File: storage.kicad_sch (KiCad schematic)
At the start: 18 parts, among them J6 Micro_SD_Card_Det1, U1 MIMX8MM6DVTLZAA, U27 TPD4EUSB30, U28 D5V0H1B2LP, U29 W25Q32JWZP, U30 SiP32431DR3, U31 TPD4EUSB30

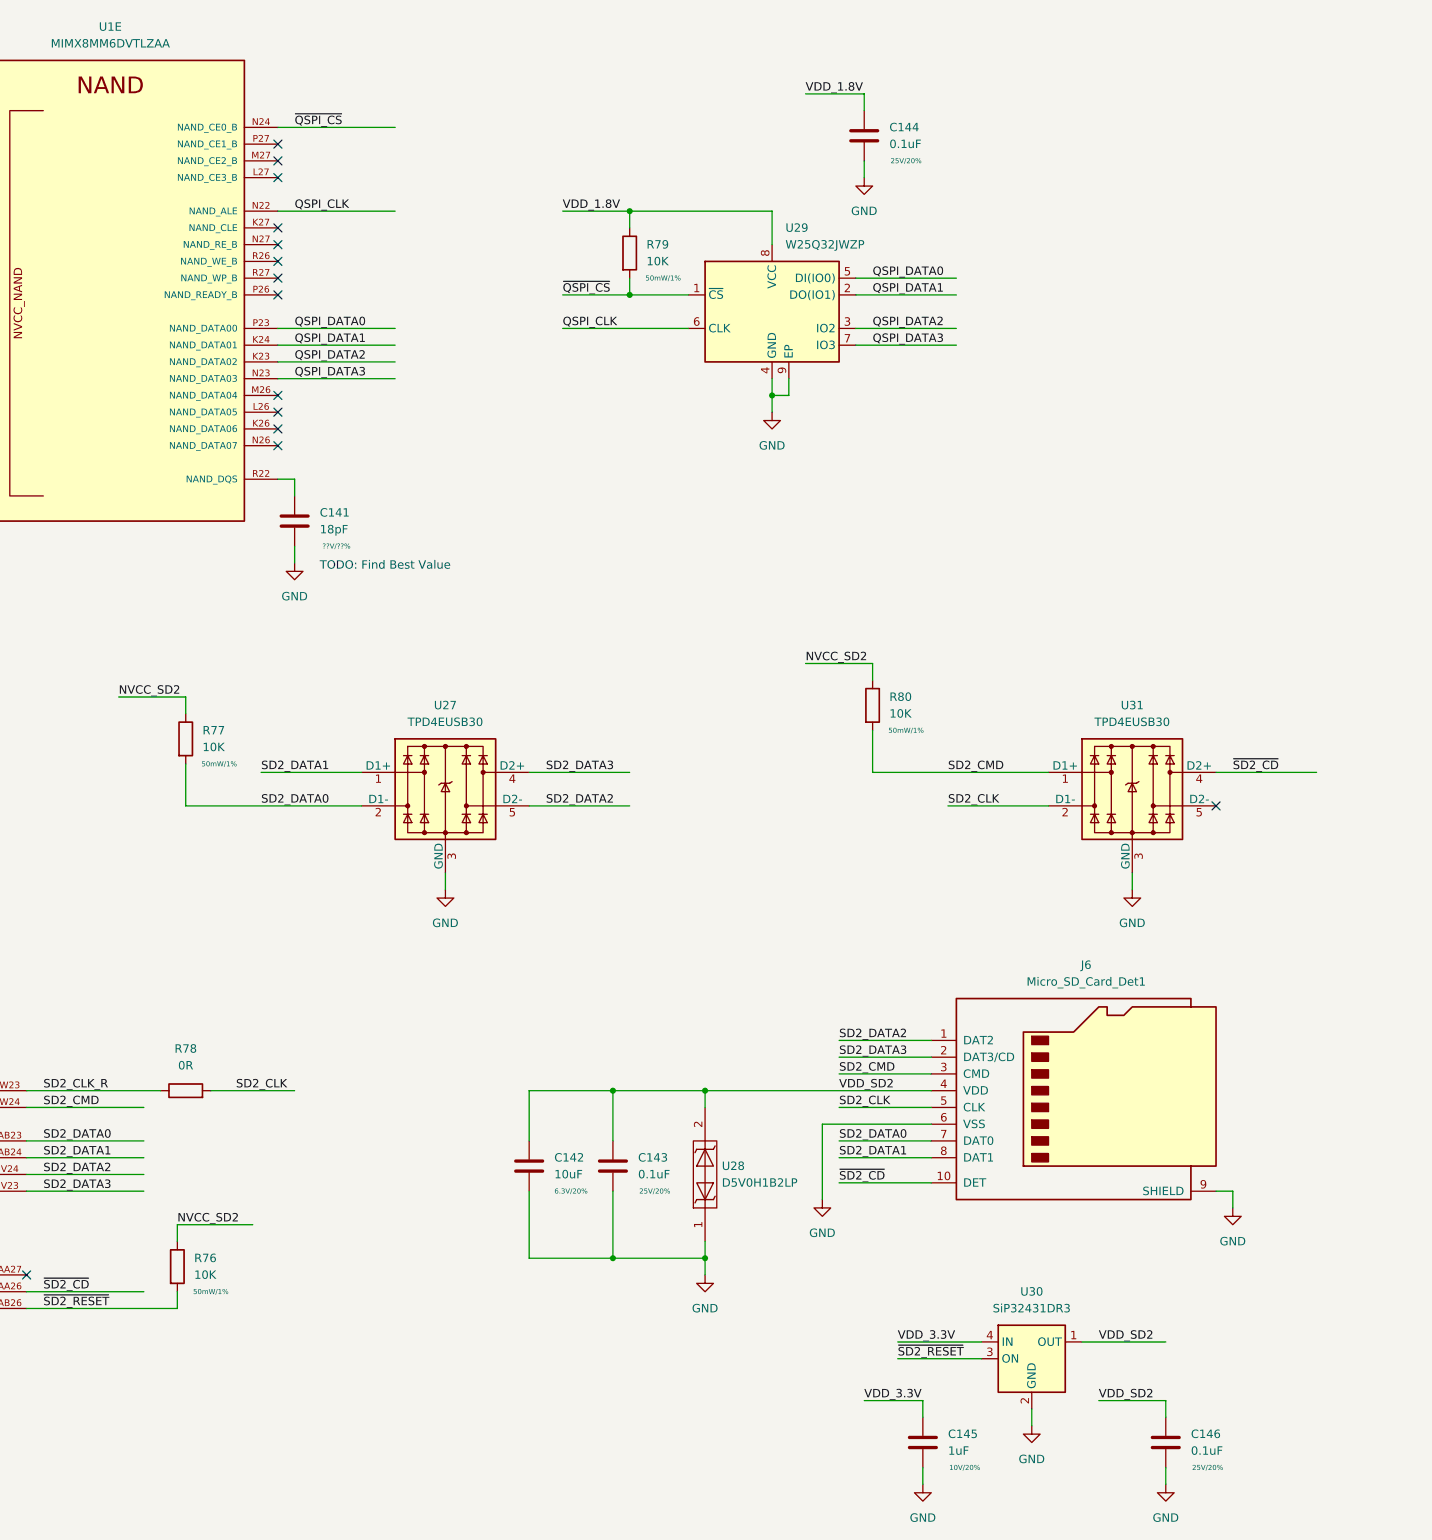
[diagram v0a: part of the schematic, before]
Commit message: v2 of ddr flytimes tool, lots of routing work, sch fixes
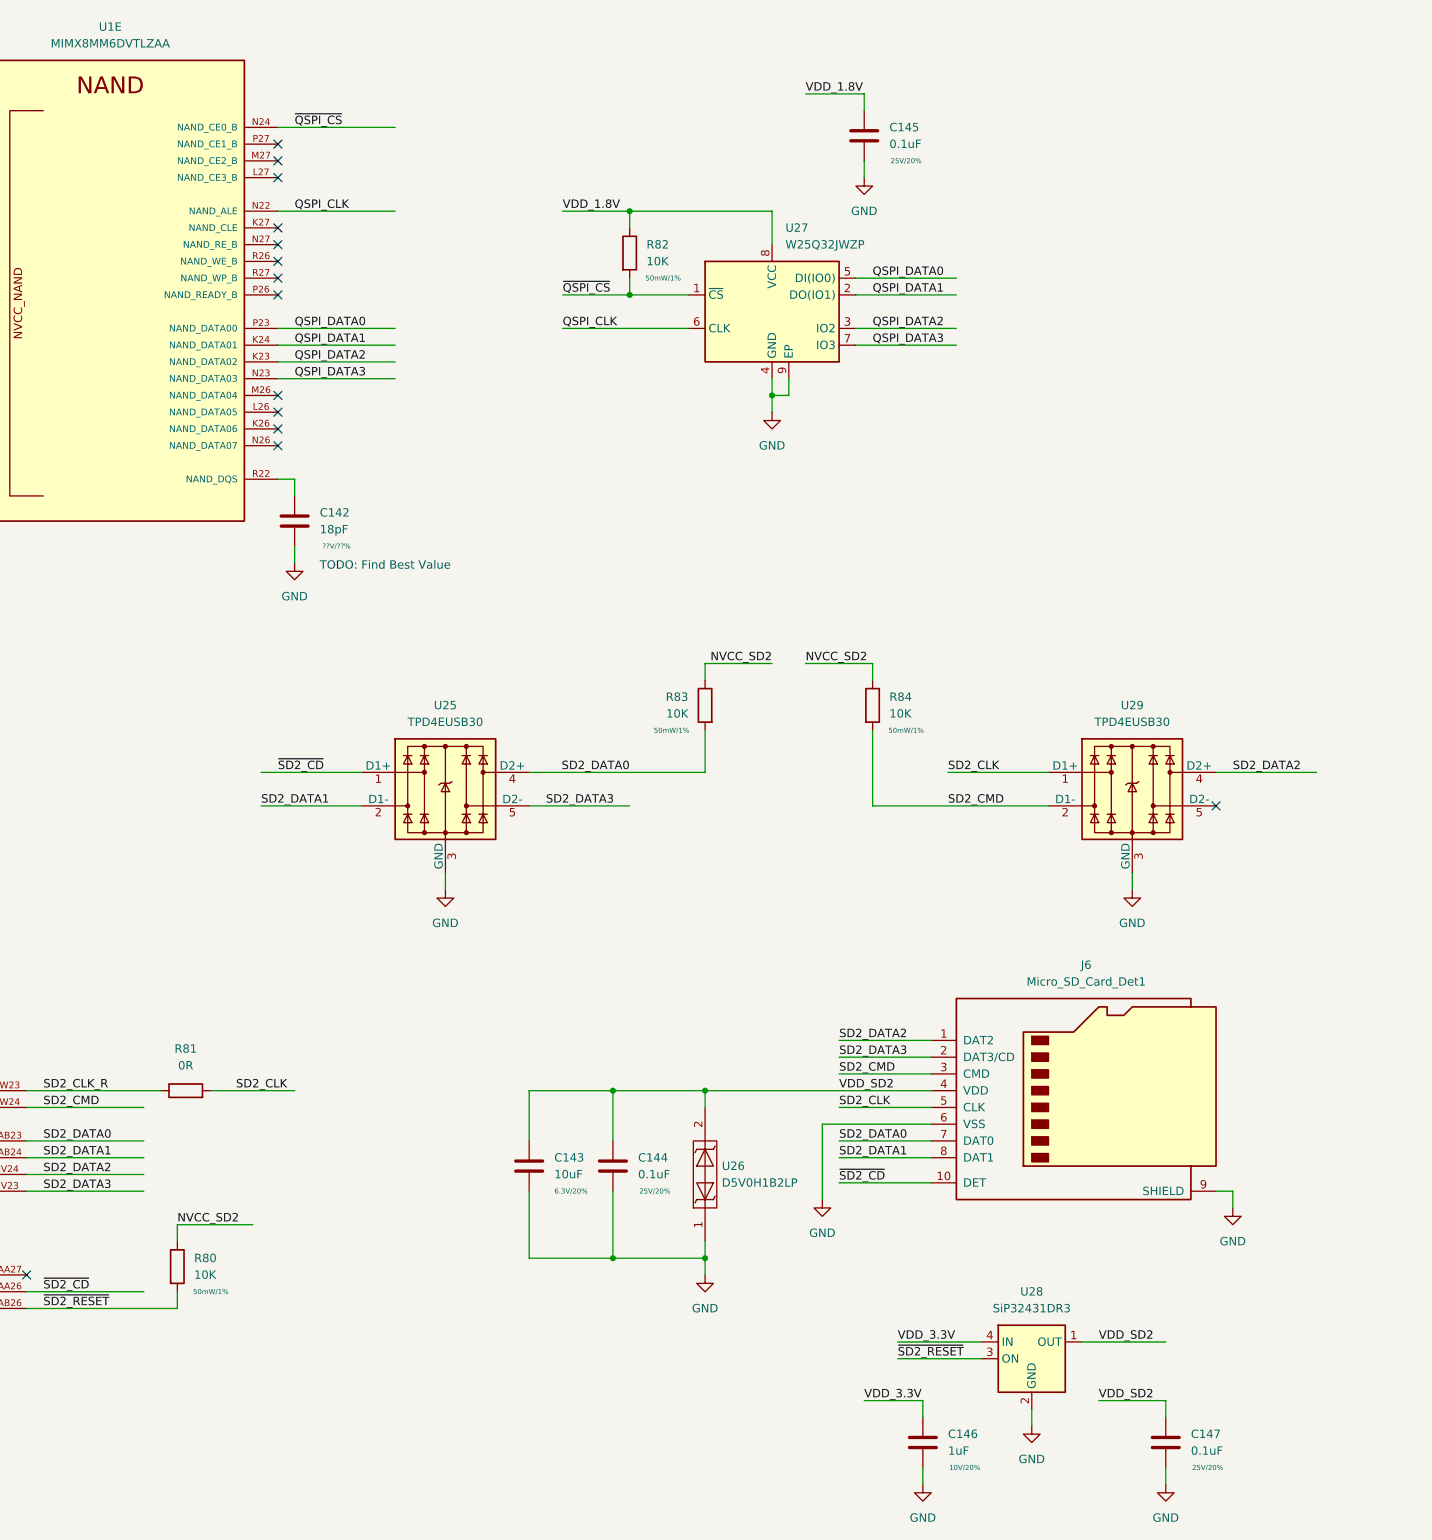
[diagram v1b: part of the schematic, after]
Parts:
- C142: renamed from C141; footprint Capacitor_SMD:C_0402_1005Metric -> qsbc:C_0201_0603Metric
- R81: renamed from R78; footprint Resistor_SMD:R_0402_1005Metric -> qsbc:R_0201_0603Metric
- renumbered C142 to C143, C143 to C144, C144 to C145, C145 to C146, C146 to C147, R76 to R80, R79 to R82, R77 to R83, R80 to R84, U27 to U25, U28 to U26, U29 to U27, U30 to U28, U31 to U29
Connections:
- net SD2_CLK: now also U29.1 (D1+), U29.10; no longer U29.2 (D1-), U29.9
- net SD2_CMD: now also U29.2 (D1-), U29.9; no longer U29.1 (D1+), U29.10
- net SD2_DATA0: now also U25.4 (D2+), U25.7; no longer U25.2 (D1-), U25.9
- net SD2_DATA1: now also U25.2 (D1-), U25.9; no longer U25.1 (D1+), U25.10
- net SD2_DATA2: now also U29.4 (D2+), U29.7; no longer U25.5 (D2-), U25.6
- net SD2_DATA3: now also U25.5 (D2-), U25.6; no longer U25.4 (D2+), U25.7
- net ~{SD2_CD}: now also U25.1 (D1+), U25.10; no longer U29.4 (D2+), U29.7
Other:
- moved on the sheet: R83

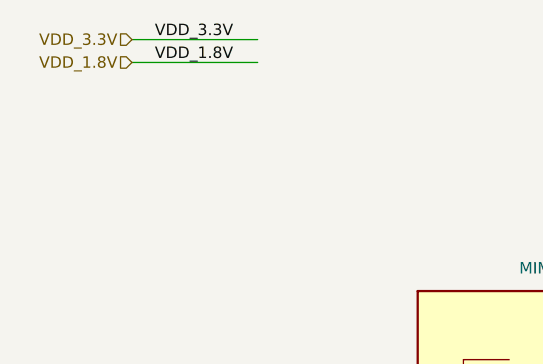
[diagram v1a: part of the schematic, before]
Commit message: more routing work, prepare to change to x32 lpddr4
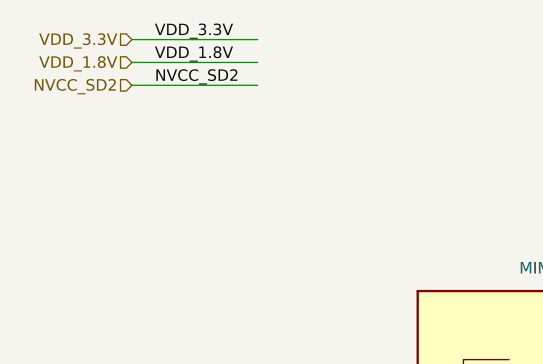
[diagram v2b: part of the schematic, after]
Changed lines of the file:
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@@
+    (stroke (width 0) (type default) (color 0 0 0 0))
+  )
+  (wire (pts (xy 29.21 24.13) (xy 43.18 24.13))
     (stroke (width 0) (type default) (color 0 0 0 0))
   )
@@
     (effects (font (size 1.27 1.27)) (justify left bottom))
   )
+  (label "NVCC_SD2" (at 31.75 24.13 0)
+    (effects (font (size 1.27 1.27)) (justify left bottom))
+  )
   (label "VDD_SD2" (at 231.14 250.19 0)
     (effects (font (size 1.27 1.27)) (justify left bottom))
@@
     (effects (font (size 1.27 1.27)) (justify right))
   )
+  (hierarchical_label "NVCC_SD2" (shape input) (at 29.21 24.13 180)
+    (effects (font (size 1.27 1.27)) (justify right))
+  )
